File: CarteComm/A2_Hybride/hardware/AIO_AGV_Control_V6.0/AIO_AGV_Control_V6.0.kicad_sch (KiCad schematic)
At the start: 59 parts, among them J1 DB25_Pins, J2 DB25_Socket, J3 Conn_Coaxial_Small, T1 IRF520, T10 IRF520, T11 IRF520, T12 IRF520, T14 IRF520, T15 IRF520, T16 IRF520, T17 IRF520, T18 IRF520, T19 IRF520, T2 IRF520, T20 IRF520, T21 IRF520, T22 IRF520, T23 IRF520, T24 IRF520, T3 IRF520, T4 IRF520, T5 IRF520, T6 IRF520, T7 IRF520, T8 IRF520, T9 IRF520, U1 ESP32-DEVKITC, U2 RFM95W-868S2

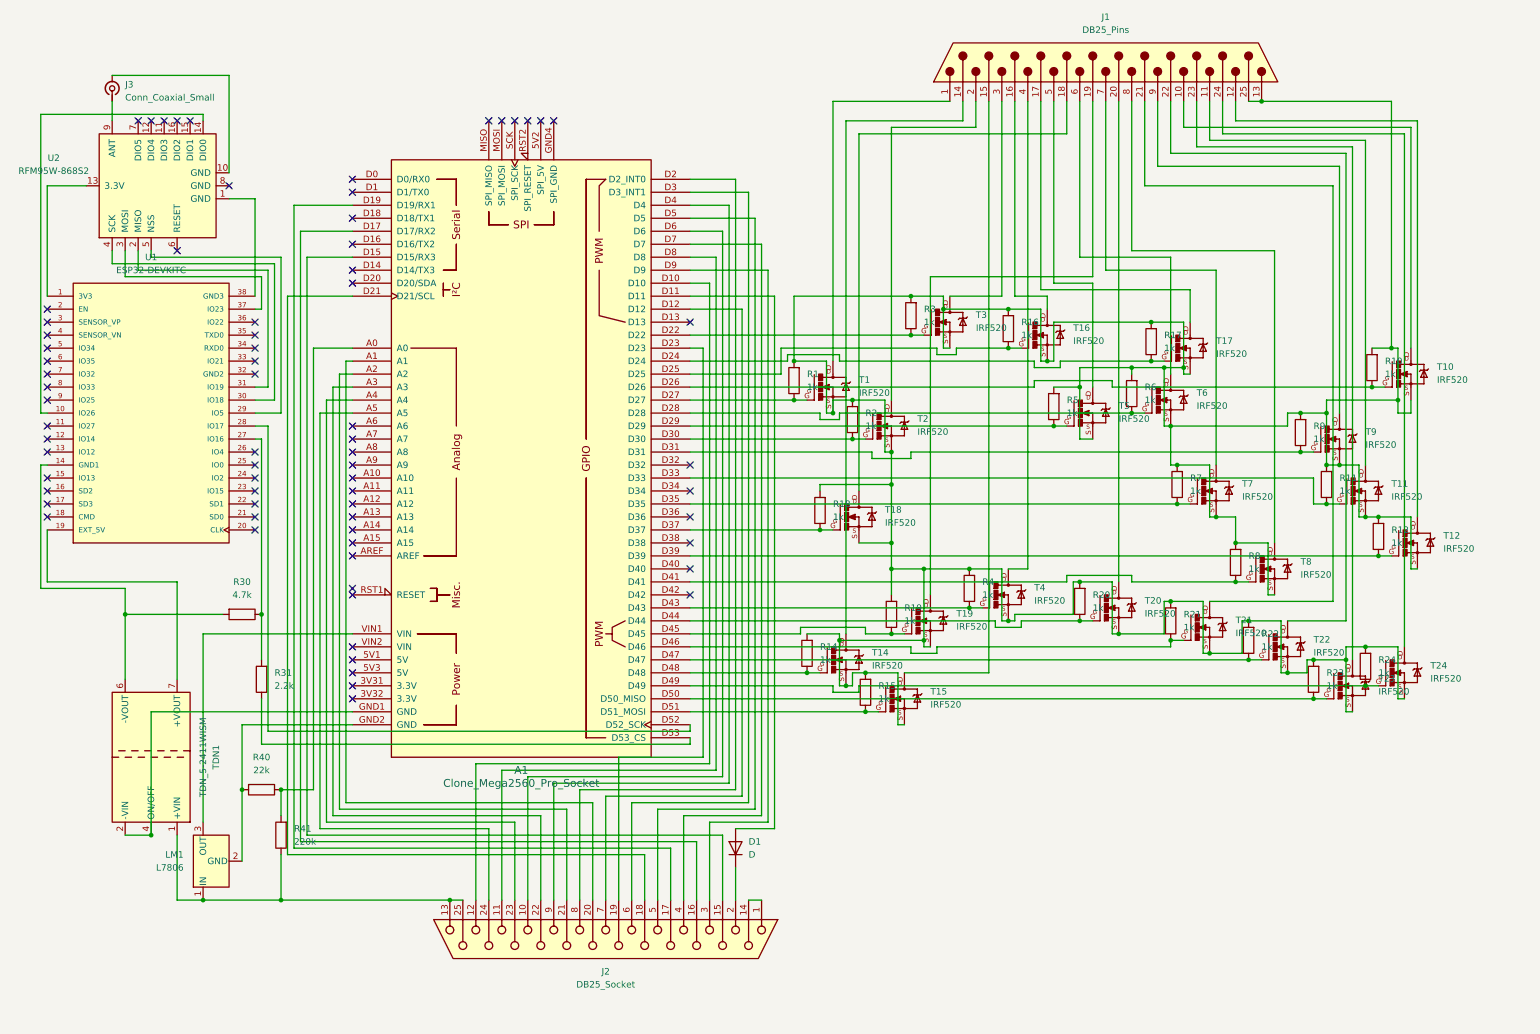
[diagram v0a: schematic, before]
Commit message: feat(banc): banc d'essai des boutons EnOcean pour UniPi E413
Service web qui enregistre les PTM 210, les détecte à l'appui ou par saisie de
l'identifiant, et ouvre une fenêtre verte à chaque pression avec le nom, le
code, l'heure et le niveau reçu.

Deux règles font la différence entre un banc utilisable et un banc qui ment. Un
PTM 210 émet TROIS sous-télégrammes par appui, et émet aussi au relâchement :
sans traitement, une pression afficherait six fenêtres. Le banc déduplique sur
(identifiant, données) dans une fenêtre de 400 ms et ne retient que le front
d'appui. Deux tests vérifient précisément cela.

Un appui non enregistré ouvre une fenêtre ambre au lieu d'être ignoré : au banc,
c'est exactement ce qu'on cherche à voir.

L'ajout par détection couvre les deux gestes réels. On peut armer la fenêtre
puis presser, mais on peut aussi avoir pressé AVANT d'ouvrir la boîte de
dialogue - le dernier appui capté est alors proposé, ce qui évite de faire le
tour de l'atelier deux fois.

Les identifiants se lisent en hexadécimal sans exception, y compris pour une
chaîne de chiffres seuls : 2732996 est un hexadécimal valide, et deviner entre
les deux bases produirait un identifiant faux une fois sur deux.

Bibliothèque standard seule hors pyserial, flux SSE, registre JSON lisible à la
main, port série détecté par lien by-id plutôt que par ttyUSB0 dont le numéro
change au rebranchement. Un mode simulation permet de tout éprouver sans
matériel.

Le banc ne dépend d'aucun dossier d'architecture : il sert à valider les boutons
avant que le choix ne soit tranché, et vaut pour A1, A2 et A4. Le décodeur ESP3
y est copié, avec la note de report réciproque.

17 tests, unité systemd durcie, README de déploiement.

Co-Authored-By: Claude Opus 5 <noreply@anthropic.com>
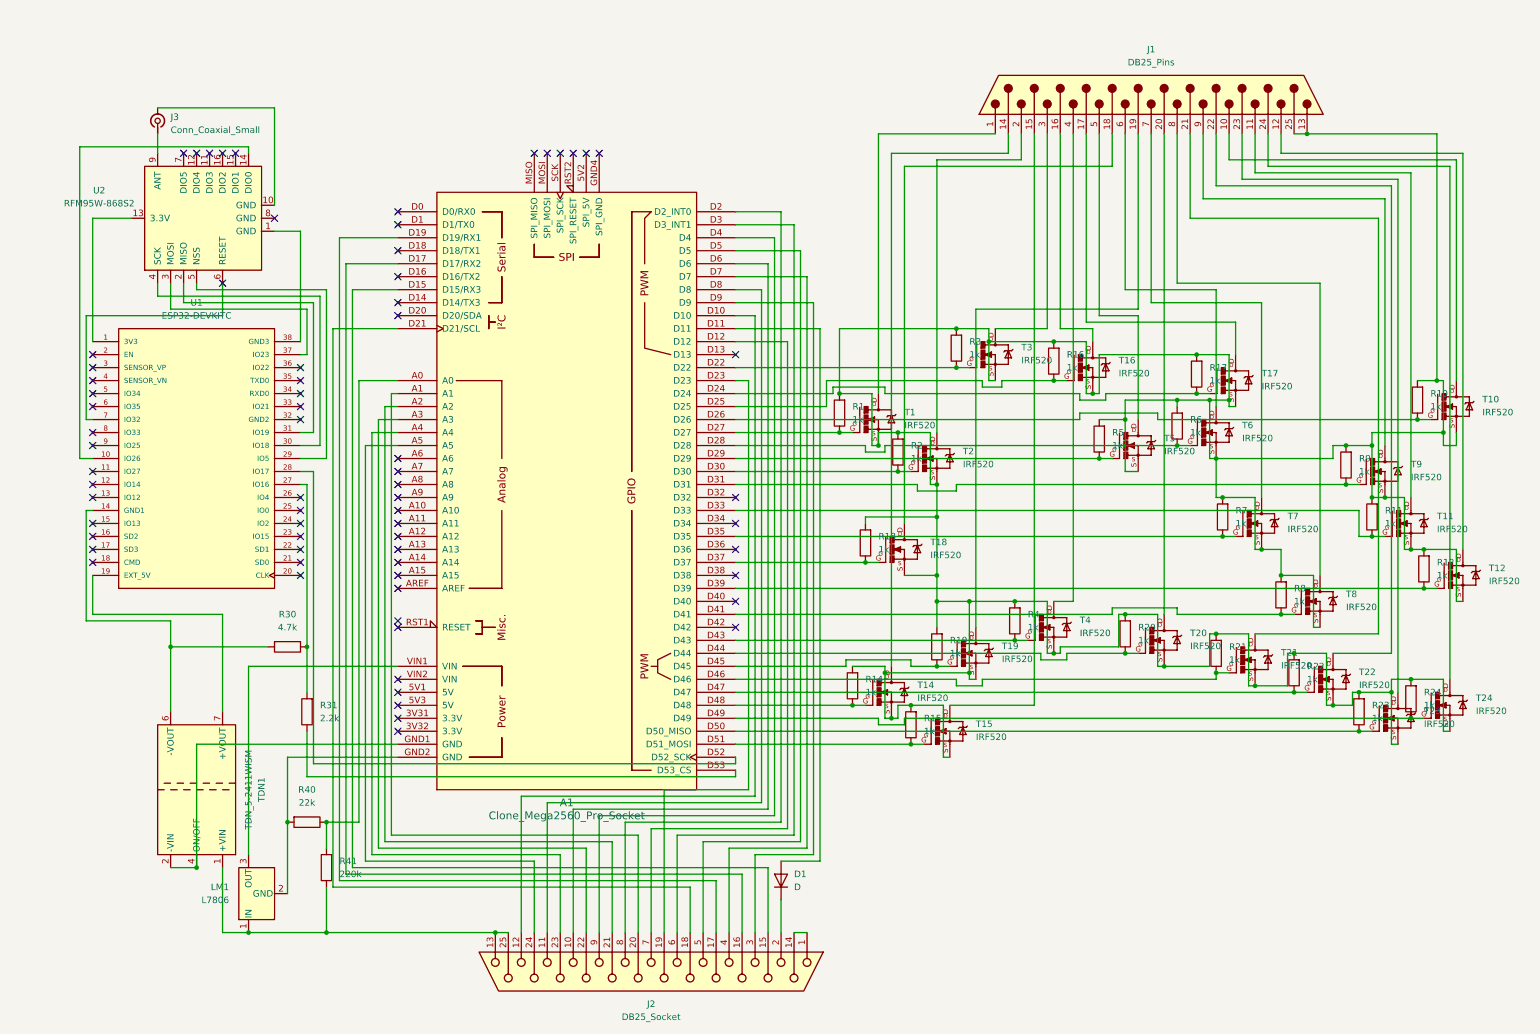
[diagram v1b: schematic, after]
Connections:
- net at U1.7 (IO32): now also U2.6 (RESET)
- no-connect marks 71 -> 70
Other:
- moved on the sheet: A1, D1, J1, J2, J3, LM1, R1, R10, R11, R12, R14, R15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
